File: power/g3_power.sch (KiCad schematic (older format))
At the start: 14 parts, among them J101 Conn_01x02_Female, J102 Conn_01x02_Female, U101 RT9471GQW, U102 TPS61202DRC

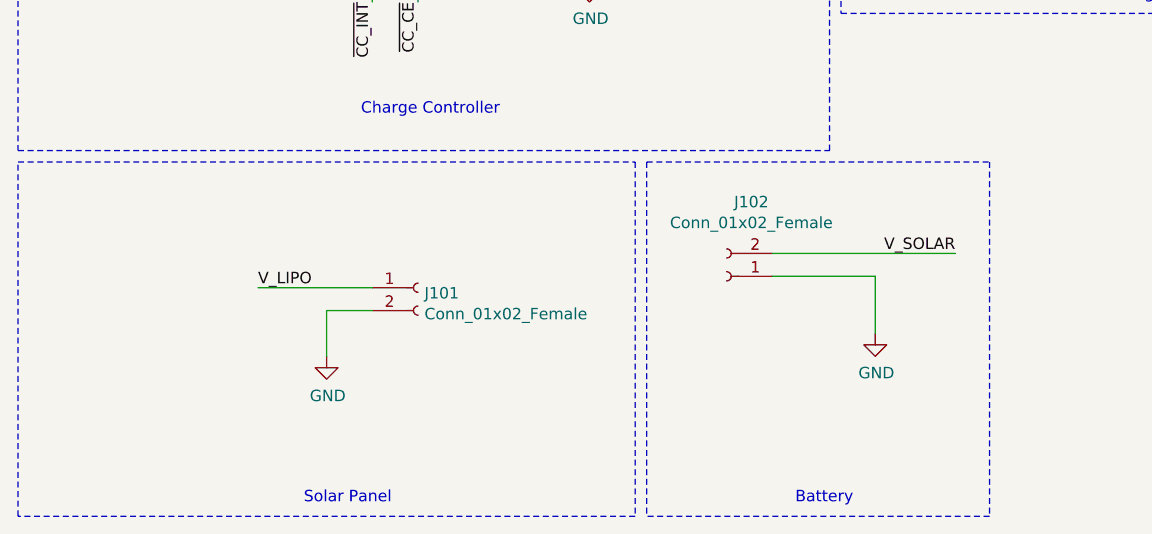
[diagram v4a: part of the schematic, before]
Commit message: small changes to power schematic layout
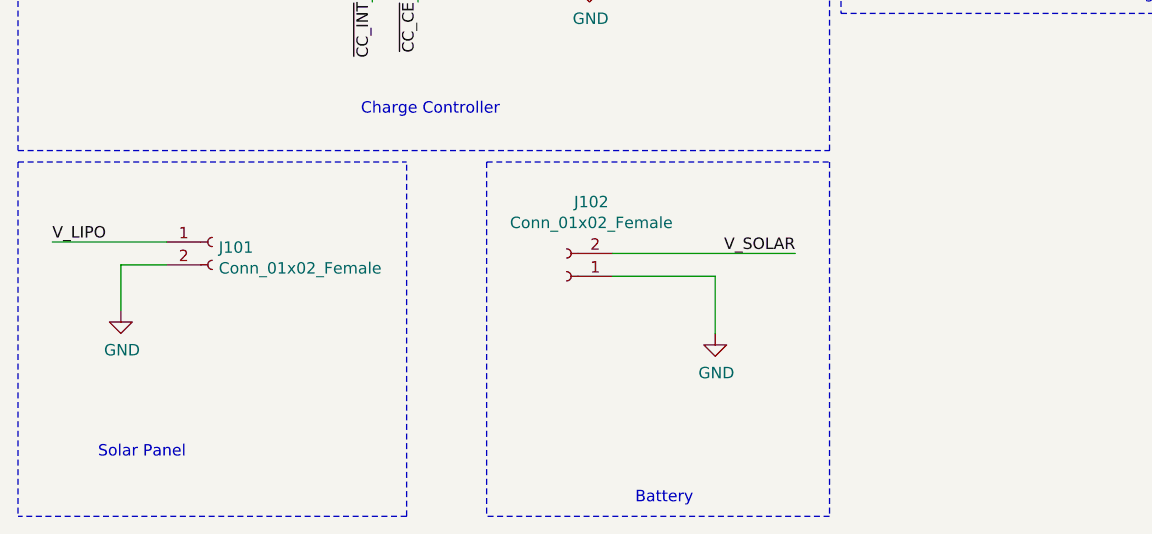
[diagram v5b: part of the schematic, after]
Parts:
- C103: Description (none) -> 4.7 uF Capacitor; MFN (none) -> Yageo; MFP (none) -> CC0402KRX5R5BB475; S1PL (none) -> https://www.digikey.com/en/products/detail/CC0402KRX5R5BB47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; S1PN (none) -> 311-3476; S2PL (none) -> https://www.mouser.com/ProductDetail/YAGEO/CC0402KRX5R5BB47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; S2PN (none) -> 603-CC0402KRX55BB475
- C104: Description (none) -> 47nF Capacitor; MFN (none) -> Yageo; MFP (none) -> CC0402KRX5R6BB473; S1PL (none) -> https://www.digikey.com/en/products/detail/CC0402KRX5R6BB47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; S1PN (none) -> 311-1688; S2PL (none) -> https://www.mouser.com/ProductDetail/YAGEO/CC0402KRX5R6BB47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; S2PN (none) -> 603-CC402KRX5R6BB473
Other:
- moved on the sheet: J101, J102
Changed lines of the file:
@@
 L Connector:Conn_01x02_Female J102
 U 1 1 61BA49C7
-P 3650 4350
-F 0 "J102" H 3542 4025 50  0000 C CNN
-F 1 "Conn_01x02_Female" H 3542 4116 50  0000 C CNN
-F 2 "" H 3650 4350 50  0001 C CNN
-F 3 "~" H 3650 4350 50  0001 C CNN
-	1    3650 4350
+P 2950 4350
+F 0 "J102" H 2842 4025 50  0000 C CNN
+F 1 "Conn_01x02_Female" H 2842 4116 50  0000 C CNN
+F 2 "" H 2950 4350 50  0001 C CNN
+F 3 "~" H 2950 4350 50  0001 C CNN
+	1    2950 4350
 	-1   0    0    1
 $EndComp
@@
 L Connector:Conn_01x02_Female J101
 U 1 1 61BA5A31
-P 2300 4400
-F 0 "J101" H 2328 4376 50  0000 L CNN
-F 1 "Conn_01x02_Female" H 2328 4285 50  0000 L CNN
-F 2 "" H 2300 4400 50  0001 C CNN
-F 3 "~" H 2300 4400 50  0001 C CNN
-	1    2300 4400
-	1    0    0    -1
-$EndComp
-Text Notes 3950 5350 0    50   ~ 0
+P 1400 4200
+F 0 "J101" H 1428 4176 50  0000 L CNN
+F 1 "Conn_01x02_Female" H 1428 4085 50  0000 L CNN
+F 2 "" H 1400 4200 50  0001 C CNN
+F 3 "~" H 1400 4200 50  0001 C CNN
+	1    1400 4200
+	1    0    0    -1
+$EndComp
+Text Notes 3250 5350 0    50   ~ 0
 Battery
-Wire Notes Line
-	3250 5400 550  5400
-Text Notes 1800 5350 0    50   ~ 0
+Text Notes 900  5150 0    50   ~ 0
 Solar Panel
 $Comp
 L power:GND #PWR0104
 U 1 1 61BA8023
-P 1900 4700
-F 0 "#PWR0104" H 1900 4450 50  0001 C CNN
-F 1 "GND" H 1905 4527 50  0000 C CNN
-F 2 "" H 1900 4700 50  0001 C CNN
-F 3 "" H 1900 4700 50  0001 C CNN
-	1    1900 4700
-	1    0    0    -1
-$EndComp
-Wire Wire Line
-	2100 4500 1900 4500
-Wire Wire Line
-	1900 4500 1900 4700
-Wire Wire Line
-	2100 4400 1600 4400
-Text Label 1600 4400 0    50   ~ 0
+P 1000 4500
+F 0 "#PWR0104" H 1000 4250 50  0001 C CNN
+F 1 "GND" H 1005 4327 50  0000 C CNN
+F 2 "" H 1000 4500 50  0001 C CNN
+F 3 "" H 1000 4500 50  0001 C CNN
+	1    1000 4500
+	1    0    0    -1
+$EndComp
+Wire Wire Line
+	1200 4300 1000 4300
+Wire Wire Line
+	1000 4300 1000 4500
+Wire Wire Line
+	1200 4200 700  4200
+Text Label 700  4200 0    50   ~ 0
 V_LIPO
 $Comp
 L power:GND #PWR0107
 U 1 1 61BAA18A
-P 4300 4600
-F 0 "#PWR0107" H 4300 4350 50  0001 C CNN
-F 1 "GND" H 4305 4427 50  0000 C CNN
-F 2 "" H 4300 4600 50  0001 C CNN
-F 3 "" H 4300 4600 50  0001 C CNN
-	1    4300 4600
-	1    0    0    -1
-$EndComp
-Wire Wire Line
-	3850 4350 4300 4350
-Wire Wire Line
-	4300 4350 4300 4600
-Wire Wire Line
-	3850 4250 4650 4250
-Text Label 4650 4250 2    50   ~ 0
+P 3600 4600
+F 0 "#PWR0107" H 3600 4350 50  0001 C CNN
+F 1 "GND" H 3605 4427 50  0000 C CNN
+F 2 "" H 3600 4600 50  0001 C CNN
+F 3 "" H 3600 4600 50  0001 C CNN
+	1    3600 4600
+	1    0    0    -1
+$EndComp
+Wire Wire Line
+	3150 4350 3600 4350
+Wire Wire Line
+	3600 4350 3600 4600
+Wire Wire Line
+	3150 4250 3950 4250
+Text Label 3950 4250 2    50   ~ 0
 V_SOLAR
 Wire Wire Line
@@
 F 1 "4.7uF" H 1765 1105 50  0000 L CNN
 F 2 "" H 1688 1000 50  0001 C CNN
-F 3 "~" H 1650 1150 50  0001 C CNN
+F 3 "https://www.yageo.com/upload/media/product/productsearch/datasheet/mlcc/UPY-GPHC_X5R_4V-to-50V_27.pdf" H 1650 1150 50  0001 C CNN
+F 4 "4.7 uF Capacitor" H 1650 1150 50  0001 C CNN "Description"
+F 5 "Yageo" H 1650 1150 50  0001 C CNN "MFN"
+F 6 "CC0402KRX5R5BB475" H 1650 1150 50  0001 C CNN "MFP"
+F 7 "https://www.digikey.com/en/products/detail/CC0402KRX5R5BB475/311-3476-1-ND/7164497?WT.z_cid=ref_netcomponents_dkc_buynow&utm_source=netcomponents&utm_medium=aggregator&utm_campaign=buynow" H 1650 1150 50  0001 C CNN "S1PL"
+F 8 "311-3476" H 1650 1150 50  0001 C CNN "S1PN"
+F 9 "https://www.mouser.com/ProductDetail/YAGEO/CC0402KRX5R5BB475?qs=UgE/0m3bTsY3XUxTV5ZyKA==&utm_source=netcomponents&utm_medium=aggregator&utm_campaign=CC0402KRX5R5BB475&utm_content=YAGEO" H 1650 1150 50  0001 C CNN "S2PL"
+F 10 "603-CC0402KRX55BB475" H 1650 1150 50  0001 C CNN "S2PN"
 	1    1650 1150
 	1    0    0    -1
@@
 F 1 "47nF" H 2400 1350 50  0000 L CNN
 F 2 "" H 2438 1300 50  0001 C CNN
-F 3 "~" H 2400 1450 50  0001 C CNN
+F 3 "https://www.yageo.com/upload/media/product/productsearch/datasheet/mlcc/UPY-GPHC_X5R_4V-to-50V_27.pdf" H 2400 1450 50  0001 C CNN
+F 4 "47nF Capacitor" H 2400 1450 50  0001 C CNN "Description"
+F 5 "Yageo" H 2400 1450 50  0001 C CNN "MFN"
+F 6 "CC0402KRX5R6BB473" H 2400 1450 50  0001 C CNN "MFP"
+F 7 "https://www.digikey.com/en/products/detail/CC0402KRX5R6BB473/311-1688-1-ND/5195590?WT.z_cid=ref_netcomponents_dkc_buynow&utm_source=netcomponents&utm_medium=aggregator&utm_campaign=buynow" H 2400 1450 50  0001 C CNN "S1PL"
+F 8 "311-1688" H 2400 1450 50  0001 C CNN "S1PN"
+F 9 "https://www.mouser.com/ProductDetail/YAGEO/CC0402KRX5R6BB473?qs=57qp5BBCQ9lqw3I8fCH4Jw==&utm_source=netcomponents&utm_medium=aggregator&utm_campaign=CC0402KRX5R6BB473&utm_content=YAGEO" H 2400 1450 50  0001 C CNN "S2PL"
+F 10 "603-CC402KRX5R6BB473" H 2400 1450 50  0001 C CNN "S2PN"
 	1    2400 1450
 	1    0    0    -1
@@
 	2950 2600 3050 2600
 Wire Notes Line
-	3300 3850 3300 5400
+	2600 3850 2600 5400
 Text Notes 2050 3650 0    50   ~ 0
 Charge Controller\n
@@
 Text Notes 5300 3150 0    50   ~ 0
 Volatge Regulator\n
-Wire Notes Line
-	550  3850 3250 3850
-Wire Notes Line
-	3250 3850 3250 5400
-Wire Notes Line
-	550  5400 550  3850
 Text Label 3750 2500 0    50   ~ 0
 CC_BAT
 Wire Notes Line
-	4800 3850 4800 5400
-Wire Notes Line
-	3300 3850 4800 3850
-Wire Notes Line
-	4800 5400 3300 5400
+	4100 3850 4100 5400
+Wire Notes Line
+	2600 3850 4100 3850
+Wire Notes Line
+	4100 5400 2600 5400
 Wire Notes Line
 	4100 3800 4100 500
@@
 Text Label 5000 1800 2    50   ~ 0
 VR_PS
+Wire Notes Line
+	2250 5400 550  5400
+Wire Notes Line
+	550  3850 550  5400
+Wire Notes Line
+	550  3850 2250 3850
+Wire Notes Line
+	2250 5400 2250 3850
 $EndSCHEMATC

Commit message: referenced charge controller footprint in schematic
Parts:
- U101: footprint (none) -> Perch:RT9471GQW
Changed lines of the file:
@@
 F 0 "U101" H 2250 2350 50  0000 L CNN
 F 1 "RT9471GQW" H 2100 2250 50  0000 L CNN
-F 2 "" H 2100 2850 50  0001 C CNN
+F 2 "Perch:RT9471GQW" H 2100 2850 50  0001 C CNN
 F 3 "https://www.richtek.com/assets/product_file/RT9471=RT9471D/DS9471D-02.pdf" H 2100 2850 50  0001 C CNN
 F 4 "Charge Controller" H 2300 2350 50  0001 C CNN "Description"

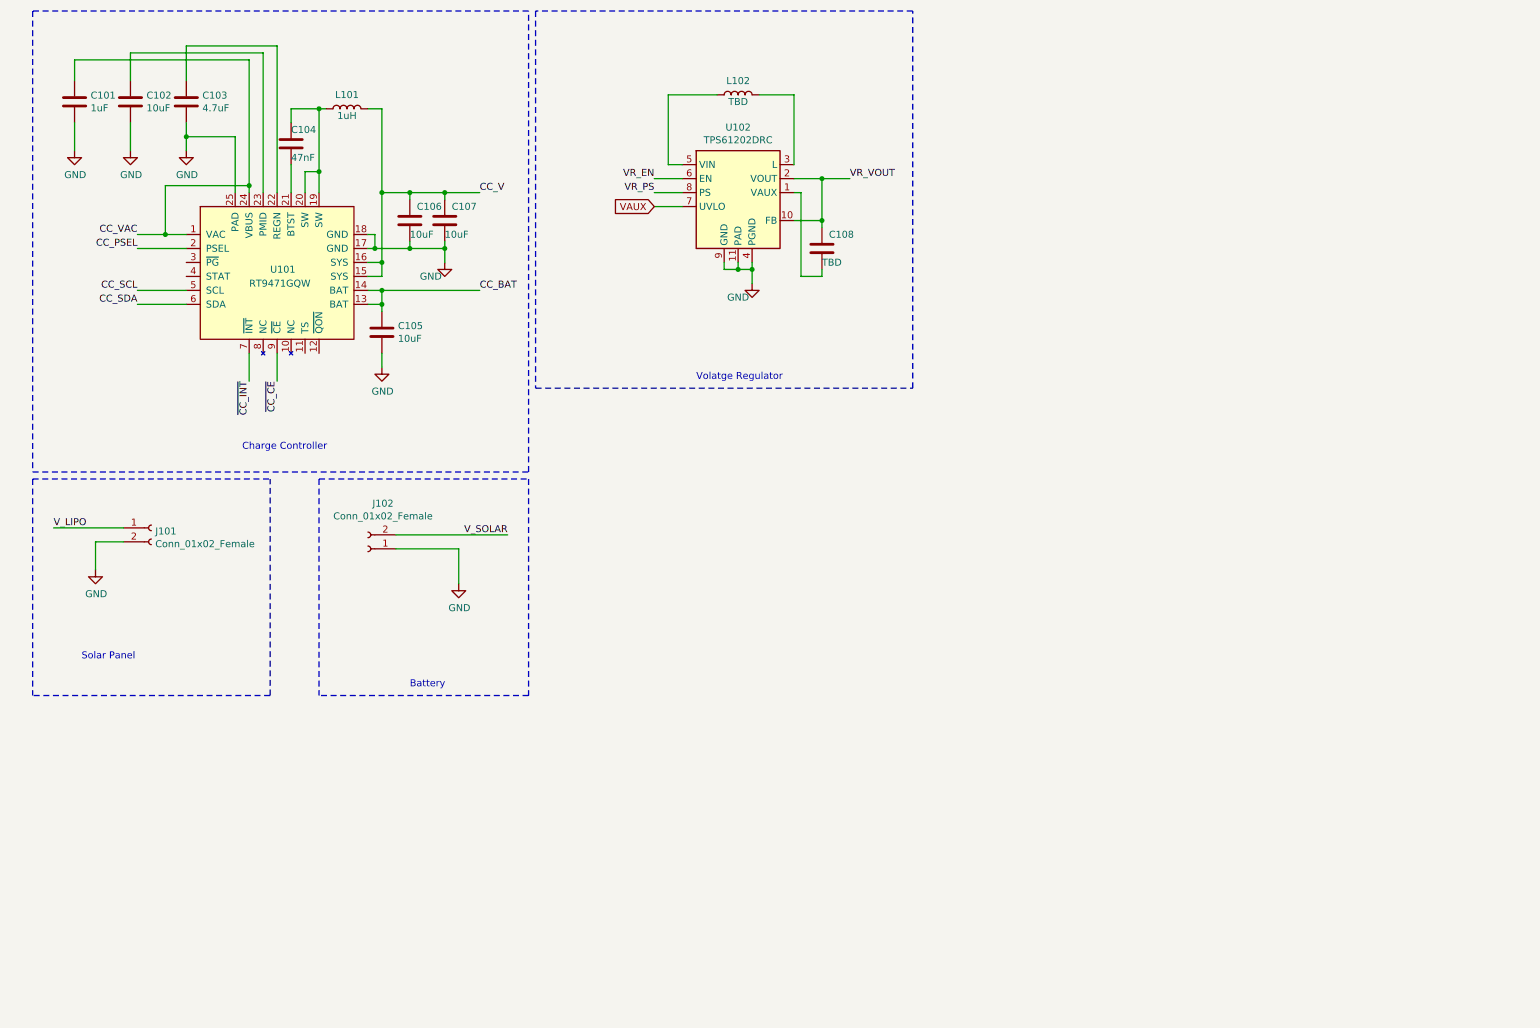
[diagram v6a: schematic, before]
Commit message: Finishing Charge Controller Implementation
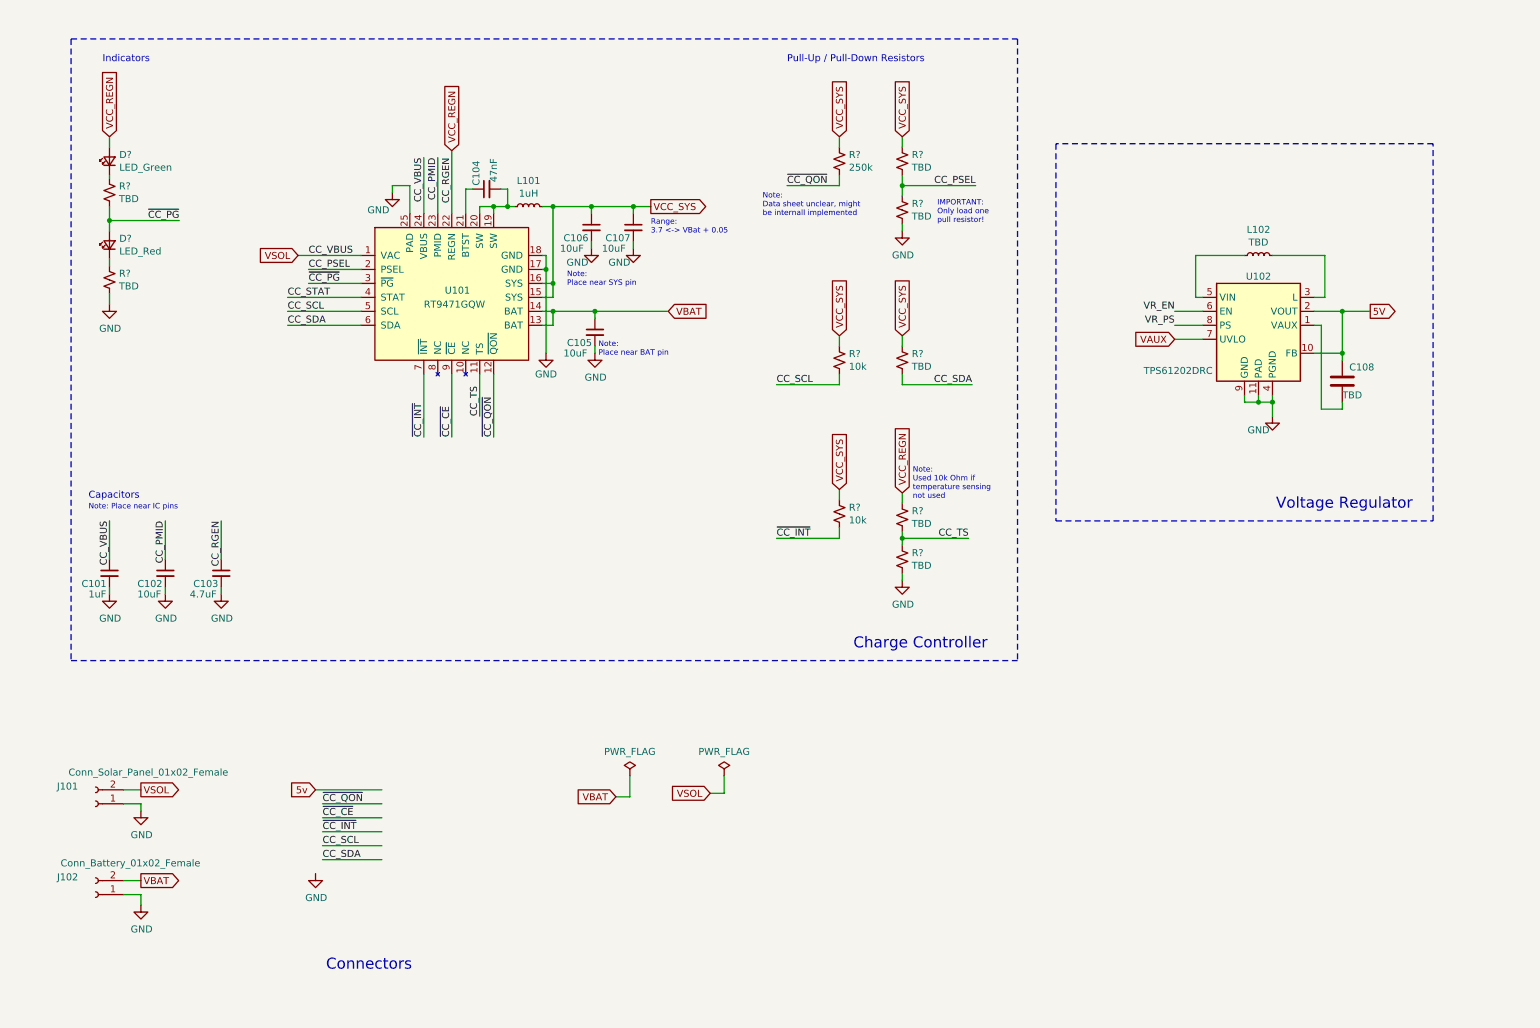
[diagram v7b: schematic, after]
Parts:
- removed C101: 1uF, symbol Device:C
- removed C102, C105, C106, C107: 10uF, symbol Device:C
- removed C103: 4.7uF, symbol Device:C
- removed C104: 47nF, symbol Device:C
- removed L101: 1uH, symbol Device:L
- removed L102: TBD, symbol Device:L
- added C101: 1uF, symbol Device:C_Small
- added C102, C105, C106, C107: 10uF, symbol Device:C_Small
- added C103: 4.7uF, symbol Device:C_Small
- added C104: 47nF, symbol Device:C_Small
- added D?: LED_Green, symbol Device:LED_Small
- added D?: LED_Red, symbol Device:LED_Small
- added L101: 1uH, symbol Device:L_Small
- added L102: TBD, symbol Device:L_Small
- added R? (x7): TBD, symbol Device:R_Small_US
- added R?: 250k, symbol Device:R_Small_US
- added R? (x2): 10k, symbol Device:R_Small_US
- J101: value Conn_01x02_Female -> Conn_Solar_Panel_01x02_Female
- J102: value Conn_01x02_Female -> Conn_Battery_01x02_Female
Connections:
- net labels added: 5V, 5v, CC_PMID, CC_RGEN, CC_STAT, CC_TS, CC_VBUS, VBAT, VCC_REGN, VCC_SYS, VSOL, ~CC_PG, ~CC_QON
- net labels removed: CC_BAT, CC_V, CC_VAC, VR_VOUT, V_LIPO, V_SOLAR
- wire segments 87 -> 123
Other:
- note added: "Capacitors"
- note added: "Connectors"
- note added: "IMPORTANT: \nOnly load one\npull resistor!"
- note added: "Indicators"
- note added: "Note: Place near IC pins"
- note added: "Note: \nData sheet unclear, might \nbe internall implemented"
- note added: "Note: \nPlace near BAT pin\n"
- note added: "Note: \nPlace near SYS pin\n"
- note added: "Note: \nUsed 10k Ohm if \ntemperature sensing \nnot used"
- note added: "Pull-Up / Pull-Down Resistors"
- note added: "Range:\n3.7 <-> VBat + 0.05"
- note added: "Voltage Regulator"
- note removed: "Battery"
- note removed: "Solar Panel"
- note removed: "Volatge Regulator\n"
- moved on the sheet: C108, J101, J102, U101, U102

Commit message: Updating Power subsystem BOM fields and board to board connector
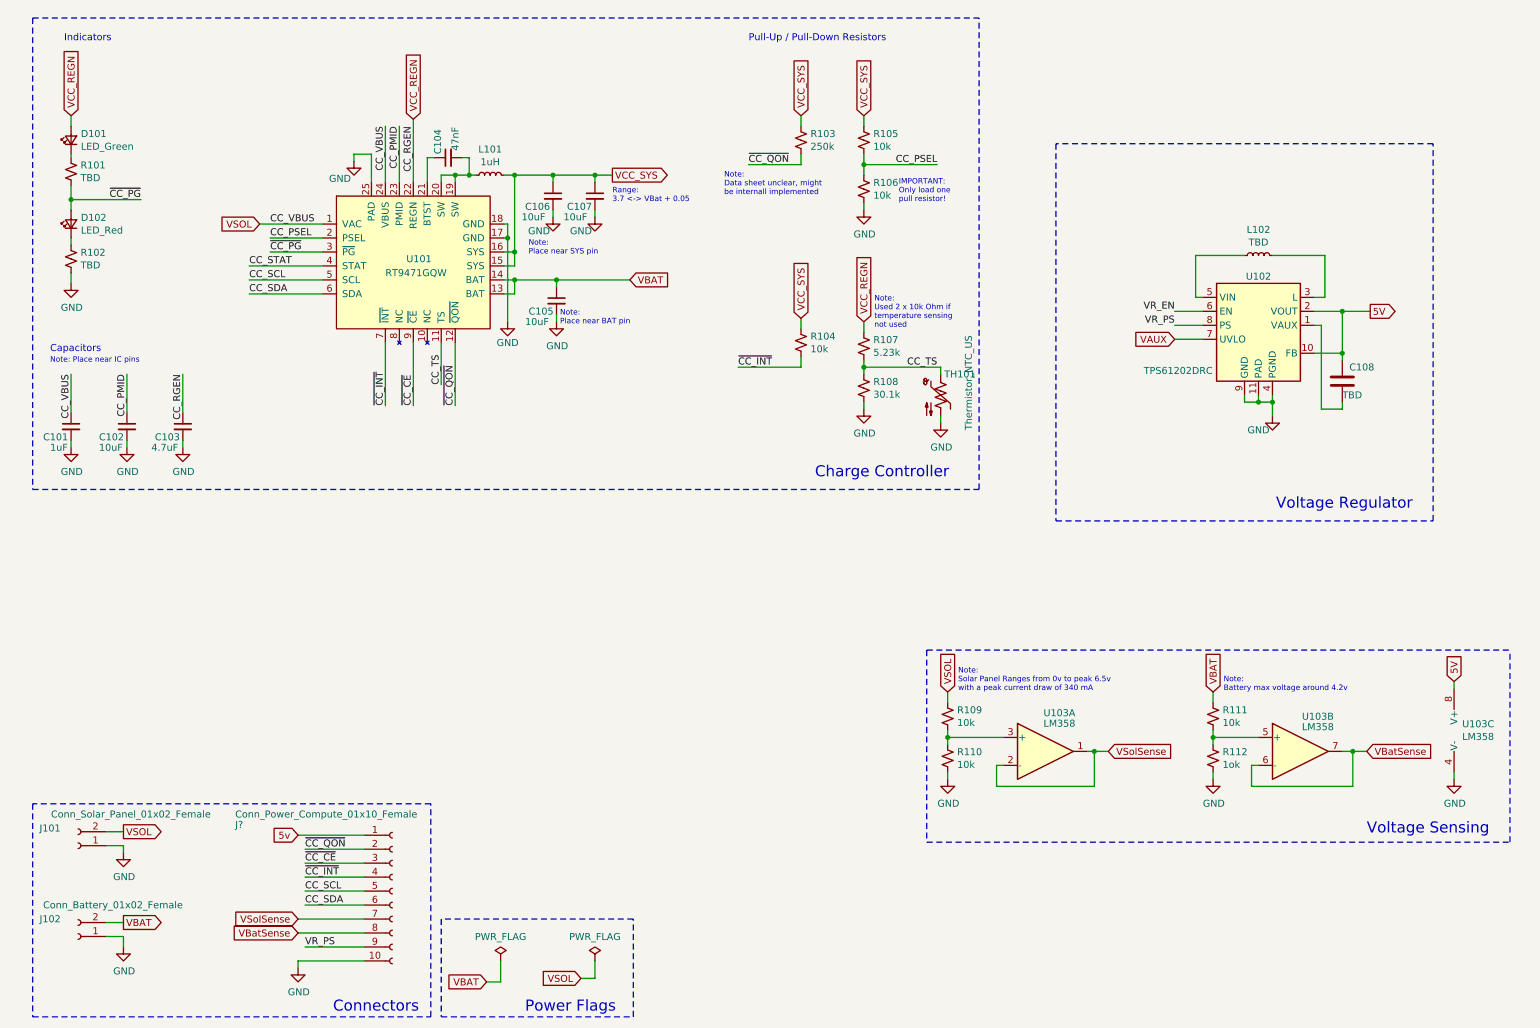
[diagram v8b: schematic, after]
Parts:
- removed R?: 10k, symbol Device:R_Small_US
- removed R?: TBD, symbol Device:R_Small_US
- added J?: Conn_Power_Compute_01x10_Female, symbol Connector:Conn_01x10_Female
- added R109, R110, R111: 10k, symbol Device:R_Small_US
- added R112: 1ok, symbol Device:R_Small_US
- added TH101: Thermistor_NTC_US, symbol Device:Thermistor_NTC_US
- added U103: LM358, symbol Amplifier_Operational:LM358
- R105, R106: renamed from R?; value TBD -> 10k
- R107: renamed from R?; value TBD -> 5.23k
- R108: renamed from R?; value TBD -> 30.1k
- gave numbers to parts that had none: 6
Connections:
- net labels added: VBatSense, VSolSense
- wire segments 123 -> 148
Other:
- note added: "Note: \nBattery max voltage around 4.2v"
- note added: "Note: \nSolar Panel Ranges from 0v to peak 6.5v \nwith a peak current draw of 340 mA"
- note added: "Note: \nUsed 2 x 10k Ohm if \ntemperature sensing \nnot used"
- note added: "Power Flags"
- note added: "Voltage Sensing"
- note removed: "Note: \nUsed 10k Ohm if \ntemperature sensing \nnot used"
- moved on the sheet: C101, C102, C103, C104, C105, C106, C107, D101, D102, J101, J102, L101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
